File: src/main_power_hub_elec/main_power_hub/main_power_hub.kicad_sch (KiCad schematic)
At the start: 43 parts, among them J101 SM02B-PASS, J6 IDC6, U102 TCAN1462V, U2 STM32G474RBT6, U4 24LC128, Y1 24MHz

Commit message: finish fixing footprints and silkscreen
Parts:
- C11, C15, C32, C33: footprint (none) -> Capacitor_SMD:C_0402_1005Metric
- D1, D13, D14, D15, D16, D2: footprint LED_SMD:LED_WS2812B-2020_PLCC4_2.0x2.0mm -> Bluesat:WS2812B-2020
- U2: footprint Package_QFP:LQFP-64-1EP_10x10mm_P0.5mm_EP5x5mm -> Bluesat:LQFP-64-0.5
- U2: footprint Package_QFP:LQFP-64_10x10mm_P0.5mm -> Bluesat:LQFP-64-0.5
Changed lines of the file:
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@@
 			)
 		)
-		(property "Footprint" "Package_QFP:LQFP-64-1EP_10x10mm_P0.5mm_EP5x5mm"
+		(property "Footprint" "Bluesat:LQFP-64-0.5"
 			(at 132.334 24.384 0)
 			(effects
@@
 			)
 		)
-		(property "Footprint" "LED_SMD:LED_WS2812B-2020_PLCC4_2.0x2.0mm"
+		(property "Footprint" "Bluesat:WS2812B-2020"
 			(at 240.03 144.78 0)
 			(effects
@@
 			)
 		)
-		(property "Footprint" ""
+		(property "Footprint" "Capacitor_SMD:C_0402_1005Metric"
 			(at 162.56 110.49 0)
 			(effects
@@
 			)
 		)
-		(property "Footprint" ""
+		(property "Footprint" "Capacitor_SMD:C_0402_1005Metric"
 			(at 162.56 68.58 0)
 			(effects
@@
 			)
 		)
-		(property "Footprint" "LED_SMD:LED_WS2812B-2020_PLCC4_2.0x2.0mm"
+		(property "Footprint" "Bluesat:WS2812B-2020"
 			(at 207.01 144.78 0)
 			(effects
@@
 			)
 		)
-		(property "Footprint" "LED_SMD:LED_WS2812B-2020_PLCC4_2.0x2.0mm"
+		(property "Footprint" "Bluesat:WS2812B-2020"
 			(at 223.52 144.78 0)
 			(effects
@@
 			)
 		)
-		(property "Footprint" "LED_SMD:LED_WS2812B-2020_PLCC4_2.0x2.0mm"
+		(property "Footprint" "Bluesat:WS2812B-2020"
 			(at 190.5 144.78 0)
 			(effects
@@
 			)
 		)
-		(property "Footprint" "Package_QFP:LQFP-64_10x10mm_P0.5mm"
+		(property "Footprint" "Bluesat:LQFP-64-0.5"
 			(at 250.444 33.274 0)
 			(effects
@@
 			)
 		)
-		(property "Footprint" ""
+		(property "Footprint" "Capacitor_SMD:C_0402_1005Metric"
 			(at 162.56 49.53 0)
 			(effects
@@
 			)
 		)
-		(property "Footprint" "LED_SMD:LED_WS2812B-2020_PLCC4_2.0x2.0mm"
+		(property "Footprint" "Bluesat:WS2812B-2020"
 			(at 256.54 144.78 0)
 			(effects
@@
 			)
 		)
-		(property "Footprint" ""
+		(property "Footprint" "Capacitor_SMD:C_0402_1005Metric"
 			(at 162.56 88.9 0)
 			(effects
@@
 			)
 		)
-		(property "Footprint" "LED_SMD:LED_WS2812B-2020_PLCC4_2.0x2.0mm"
+		(property "Footprint" "Bluesat:WS2812B-2020"
 			(at 173.99 144.78 0)
 			(effects

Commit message: Perfect DRC pass, no errors
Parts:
- removed D10: D_TVS_Dual_Compact, Package_DFN_QFN:Diodes_UDFN-10_1.0x2.5mm_P0.5mm, symbol Bluesat:D_TVS_Quad_Compact
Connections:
- no-connect marks 1 -> 5
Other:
- note added: "TVS WAS HERE RIP"
- note removed: "change TVS during layout whats easiest"
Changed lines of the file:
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@@
 		)
 	)
-	(text "change TVS during layout\nwhats easiest"
+	(text "TVS WAS HERE\nRIP"
 		(exclude_from_sim no)
-		(at 46.99 96.266 0)
+		(at 44.704 88.9 0)
 		(effects
 			(font
@@
 	)
 	(no_connect
+		(at 45.72 83.82)
+	)
+	(no_connect
+		(at 48.26 83.82)
+	)
+	(no_connect
 		(at 262.89 137.16)
 	)
+	(no_connect
+		(at 40.64 83.82)
+	)
+	(no_connect
+		(at 43.18 83.82)
+	)
 	(bus_entry
 		(at 33.02 69.85)
@@
 	(wire
 		(pts
-			(xy 44.45 97.79) (xy 44.45 91.44)
-		)
-		(stroke
-			(width 0)
-			(type default)
-		)
-	)
-	(wire
-		(pts
 			(xy 205.74 128.27) (xy 222.25 128.27)
 		)
@@
 	)
 	(symbol
-		(lib_id "Bluesat:D_TVS_Quad_Compact")
-		(at 44.45 87.63 0)
-		(unit 1)
-		(exclude_from_sim no)
-		(in_bom yes)
-		(on_board yes)
-		(dnp no)
-		(property "Reference" "D10"
-			(at 35.306 89.662 0)
-			(effects
-				(font
-					(size 1.016 1.016)
-				)
-				(justify left)
-			)
-		)
-		(property "Value" "D_TVS_Dual_Compact"
-			(at 35.306 92.202 0)
-			(effects
-				(font
-					(size 1.016 1.016)
-				)
-				(justify left)
-			)
-		)
-		(property "Footprint" "Package_DFN_QFN:Diodes_UDFN-10_1.0x2.5mm_P0.5mm"
-			(at 44.45 87.63 0)
-			(effects
-				(font
-					(size 1.27 1.27)
-				)
-				(hide yes)
-			)
-		)
-		(property "Datasheet" "~"
-			(at 44.45 87.63 0)
-			(effects
-				(font
-					(size 1.27 1.27)
-				)
-				(hide yes)
-			)
-		)
-		(property "Description" "Dual bidirectional transient-voltage-suppression diode, compact symbol"
-			(at 44.45 87.63 0)
-			(effects
-				(font
-					(size 1.27 1.27)
-				)
-				(hide yes)
-			)
-		)
-		(pin "10"
-		)
-		(pin "3"
-		)
-		(pin "9"
-		)
-		(pin "2"
-		)
-		(pin "1"
-		)
-		(pin "6"
-		)
-		(pin "5"
-		)
-		(pin "4"
-		)
-		(pin "8"
-		)
-		(pin "7"
-		)
-		(instances
-			(project "main_power_hub"
-				(path "/535f321e-8428-4dab-8e55-8d6d7e9876bc"
-					(reference "D10")
-					(unit 1)
-				)
-			)
-		)
-	)
-	(symbol
 		(lib_id "Device:Crystal_GND24_Small")
 		(at 99.06 57.15 270)
@@
 					(unit 1)
 				)
-			)
-		)
-	)
-	(symbol
-		(lib_id "power:GND")
-		(at 44.45 97.79 0)
-		(unit 1)
-		(exclude_from_sim no)
-		(in_bom yes)
-		(on_board yes)
-		(dnp no)
-		(fields_autoplaced yes)
-		(property "Reference" "#PWR046"
-			(at 44.45 104.14 0)
-			(effects
-				(font
-					(size 1.27 1.27)
-				)
-				(hide yes)
-			)
-		)
-		(property "Value" "GND"
-			(at 44.45 102.87 0)
-			(effects
-				(font
-					(size 1.27 1.27)
-				)
-			)
-		)
-		(property "Footprint" ""
-			(at 44.45 97.79 0)
-			(effects
-				(font
-					(size 1.27 1.27)
-				)
-				(hide yes)
-			)
-		)
-		(property "Datasheet" ""
-			(at 44.45 97.79 0)
-			(effects
-				(font
-					(size 1.27 1.27)
-				)
-				(hide yes)
-			)
-		)
-		(property "Description" "Power symbol creates a global label with name \"GND\" , ground"
-			(at 44.45 97.79 0)
-			(effects
-				(font
-					(size 1.27 1.27)
-				)
-				(hide yes)
-			)
-		)
-		(pin "1"
-		)
-		(instances
-			(project "main_power_hub"
-				(path "/535f321e-8428-4dab-8e55-8d6d7e9876bc"
-					(reference "#PWR046")
-					(unit 1)
-				)

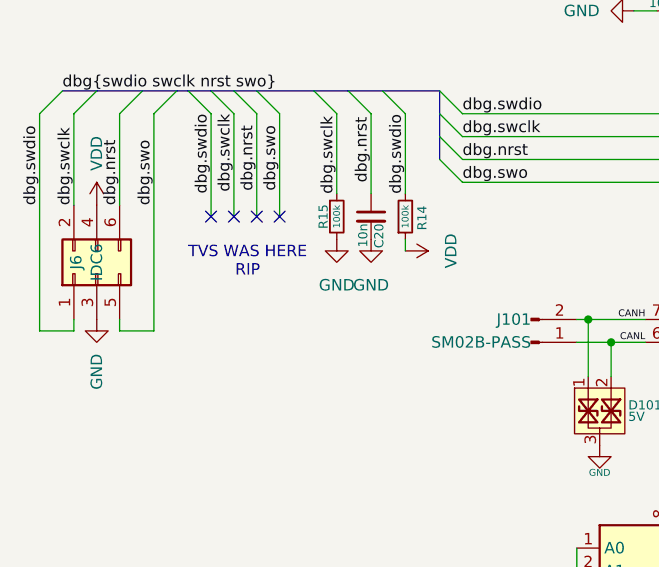
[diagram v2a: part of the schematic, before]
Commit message: TVS Diode back
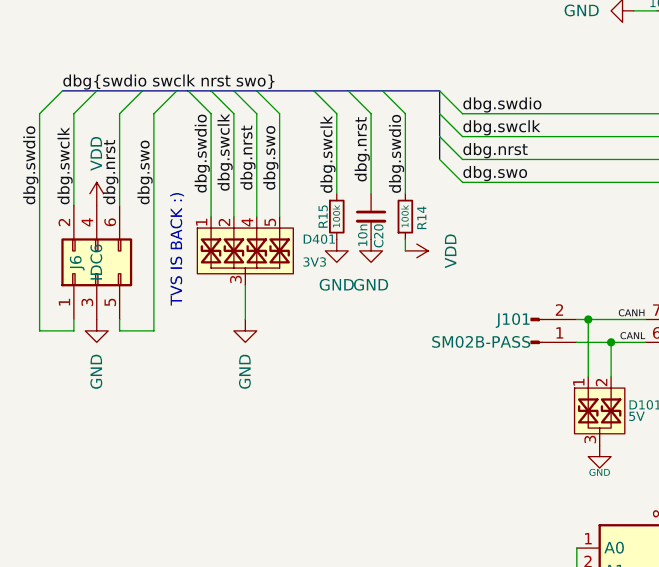
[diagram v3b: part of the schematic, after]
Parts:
- added D401: 3V3, Package_DFN_QFN:Diodes_UDFN-10_1.0x2.5mm_P0.5mm, symbol Bluesat:D_TVS_Quad_Compact
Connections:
- net GND: now also D401.3, D401.8
- net dbg.nrst: now also D401.4, D401.7
- net dbg.swclk: now also D401.2, D401.9
- net dbg.swdio: now also D401.1, D401.10
- net dbg.swo: now also D401.5, D401.6
- no-connect marks 5 -> 1
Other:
- note added: "TVS IS BACK :)"
- note removed: "TVS WAS HERE RIP"
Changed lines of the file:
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@@
 		)
 	)
-	(text "TVS WAS HERE\nRIP"
+	(text "TVS IS BACK :)"
 		(exclude_from_sim no)
-		(at 44.704 88.9 0)
+		(at 36.83 87.63 90)
 		(effects
 			(font
@@
 	)
 	(no_connect
-		(at 45.72 83.82)
-	)
-	(no_connect
-		(at 48.26 83.82)
-	)
-	(no_connect
 		(at 262.89 137.16)
 	)
-	(no_connect
-		(at 40.64 83.82)
-	)
-	(no_connect
-		(at 43.18 83.82)
-	)
 	(bus_entry
 		(at 33.02 69.85)
@@
 	(wire
 		(pts
+			(xy 44.45 95.25) (xy 44.45 91.44)
+		)
+		(stroke
+			(width 0)
+			(type default)
+		)
+	)
+	(wire
+		(pts
 			(xy 246.38 137.16) (xy 247.65 137.16)
 		)
@@
 	)
 	(symbol
+		(lib_id "Bluesat:D_TVS_Quad_Compact")
+		(at 44.45 87.63 0)
+		(unit 1)
+		(exclude_from_sim no)
+		(in_bom yes)
+		(on_board yes)
+		(dnp no)
+		(property "Reference" "D401"
+			(at 50.8 86.3599 0)
+			(effects
+				(font
+					(size 1.016 1.016)
+				)
+				(justify left)
+			)
+		)
+		(property "Value" "3V3"
+			(at 50.8 88.8999 0)
+			(effects
+				(font
+					(size 1.016 1.016)
+				)
+				(justify left)
+			)
+		)
+		(property "Footprint" "Package_DFN_QFN:Diodes_UDFN-10_1.0x2.5mm_P0.5mm"
+			(at 44.45 87.63 0)
+			(effects
+				(font
+					(size 1.27 1.27)
+				)
+				(hide yes)
+			)
+		)
+		(property "Datasheet" "~"
+			(at 44.45 87.63 0)
+			(effects
+				(font
+					(size 1.27 1.27)
+				)
+				(hide yes)
+			)
+		)
+		(property "Description" "Dual bidirectional transient-voltage-suppression diode, compact symbol"
+			(at 44.45 87.63 0)
+			(effects
+				(font
+					(size 1.27 1.27)
+				)
+				(hide yes)
+			)
+		)
+		(pin "2"
+		)
+		(pin "10"
+		)
+		(pin "3"
+		)
+		(pin "1"
+		)
+		(pin "4"
+		)
+		(pin "8"
+		)
+		(pin "7"
+		)
+		(pin "9"
+		)
+		(pin "6"
+		)
+		(pin "5"
+		)
+		(instances
+			(project "main_power_hub"
+				(path "/535f321e-8428-4dab-8e55-8d6d7e9876bc"
+					(reference "D401")
+					(unit 1)
+				)
+			)
+		)
+	)
+	(symbol
 		(lib_id "Device:Crystal_GND24_Small")
 		(at 99.06 57.15 270)
@@
 					(unit 1)
 				)
+			)
+		)
+	)
+	(symbol
+		(lib_id "power:GND")
+		(at 44.45 95.25 0)
+		(unit 1)
+		(exclude_from_sim no)
+		(in_bom yes)
+		(on_board yes)
+		(dnp no)
+		(fields_autoplaced yes)
+		(property "Reference" "#PWR0101"
+			(at 44.45 101.6 0)
+			(effects
+				(font
+					(size 1.27 1.27)
+				)
+				(hide yes)
+			)
+		)
+		(property "Value" "GND"
+			(at 44.4499 99.06 90)
+			(effects
+				(font
+					(size 1.27 1.27)
+				)
+				(justify right)
+			)
+		)
+		(property "Footprint" ""
+			(at 44.45 95.25 0)
+			(effects
+				(font
+					(size 1.27 1.27)
+				)
+				(hide yes)
+			)
+		)
+		(property "Datasheet" ""
+			(at 44.45 95.25 0)
+			(effects
+				(font
+					(size 1.27 1.27)
+				)
+				(hide yes)
+			)
+		)
+		(property "Description" "Power symbol creates a global label with name \"GND\" , ground"
+			(at 44.45 95.25 0)
+			(effects
+				(font
+					(size 1.27 1.27)
+				)
+				(hide yes)
+			)
+		)
+		(pin "1"
+		)
+		(instances
+			(project "main_power_hub"
+				(path "/535f321e-8428-4dab-8e55-8d6d7e9876bc"
+					(reference "#PWR0101")
+					(unit 1)
+				)

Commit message: Update swdebug header
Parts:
- added H1, H2: MountingHole, Bluesat:M2.5, symbol Mechanical:MountingHole
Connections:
- net dbg.nrst: now also J6.5 (Pin_5); no longer J6.6 (Pin_6)
- net dbg.swclk: now also J6.1 (Pin_1); no longer J6.2 (Pin_2)
- net dbg.swdio: now also J6.2 (Pin_2); no longer J6.1 (Pin_1)
- net dbg.swo: now also J6.6 (Pin_6); no longer J6.5 (Pin_5)
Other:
- moved on the sheet: J6

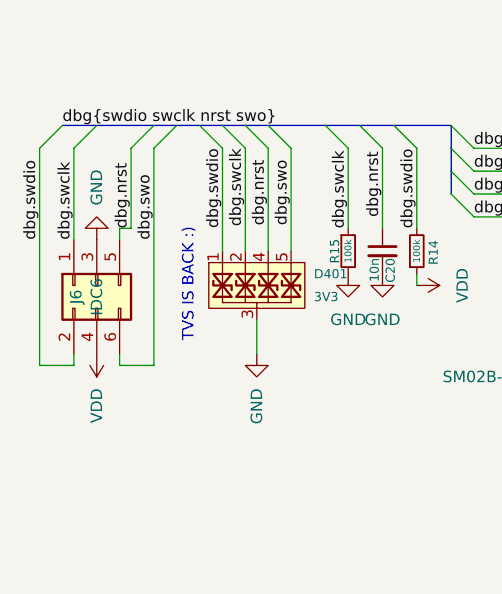
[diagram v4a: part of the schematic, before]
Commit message: Fix IDC6 pinout
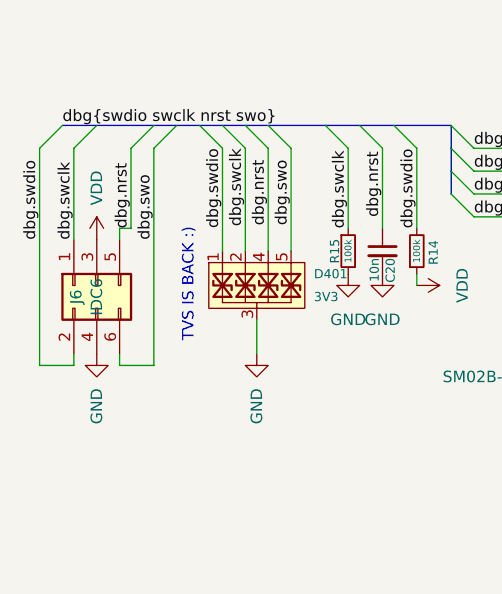
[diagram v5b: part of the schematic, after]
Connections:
- net GND: now also J6.4 (Pin_4); no longer J6.3 (Pin_3)
- net VDD: now also J6.3 (Pin_3); no longer J6.4 (Pin_4)
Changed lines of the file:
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@@
 	(symbol
 		(lib_id "power:GND")
-		(at 26.67 82.55 0)
-		(mirror x)
+		(at 26.67 95.25 0)
 		(unit 1)
 		(exclude_from_sim no)
@@
 		(fields_autoplaced yes)
 		(property "Reference" "#PWR036"
-			(at 26.67 76.2 0)
+			(at 26.67 101.6 0)
 			(effects
 				(font
@@
 		)
 		(property "Value" "GND"
-			(at 26.6699 78.74 90)
+			(at 26.6699 99.06 90)
 			(effects
 				(font
@@
 		)
 		(property "Footprint" ""
-			(at 26.67 82.55 0)
+			(at 26.67 95.25 0)
 			(effects
 				(font
@@
 		)
 		(property "Datasheet" ""
-			(at 26.67 82.55 0)
+			(at 26.67 95.25 0)
 			(effects
 				(font
@@
 		)
 		(property "Description" "Power symbol creates a global label with name \"GND\" , ground"
-			(at 26.67 82.55 0)
+			(at 26.67 95.25 0)
 			(effects
 				(font
@@
 	(symbol
 		(lib_id "power:VDD")
-		(at 26.67 95.25 0)
-		(mirror x)
+		(at 26.67 82.55 0)
 		(unit 1)
 		(exclude_from_sim no)
@@
 		(fields_autoplaced yes)
 		(property "Reference" "#PWR037"
-			(at 26.67 91.44 0)
+			(at 26.67 86.36 0)
 			(effects
 				(font
@@
 		)
 		(property "Value" "VDD"
-			(at 26.6699 99.06 90)
+			(at 26.6699 78.74 90)
 			(effects
 				(font
@@
 		)
 		(property "Footprint" ""
-			(at 26.67 95.25 0)
+			(at 26.67 82.55 0)
 			(effects
 				(font
@@
 		)
 		(property "Datasheet" ""
-			(at 26.67 95.25 0)
+			(at 26.67 82.55 0)
 			(effects
 				(font
@@
 		)
 		(property "Description" "Power symbol creates a global label with name \"VDD\""
-			(at 26.67 95.25 0)
+			(at 26.67 82.55 0)
 			(effects
 				(font

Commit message: Use bluesat TSSOP8 footprint
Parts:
- U4: footprint Package_SO:TSSOP-8_4.4x3mm_P0.65mm -> Bluesat:TSSOP-8_4.4x3.0-0.65
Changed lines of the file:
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@@
 			)
 		)
-		(property "Footprint" "Package_SO:TSSOP-8_4.4x3mm_P0.65mm"
+		(property "Footprint" "Bluesat:TSSOP-8_4.4x3.0-0.65"
 			(at 91.44 123.19 0)
 			(effects

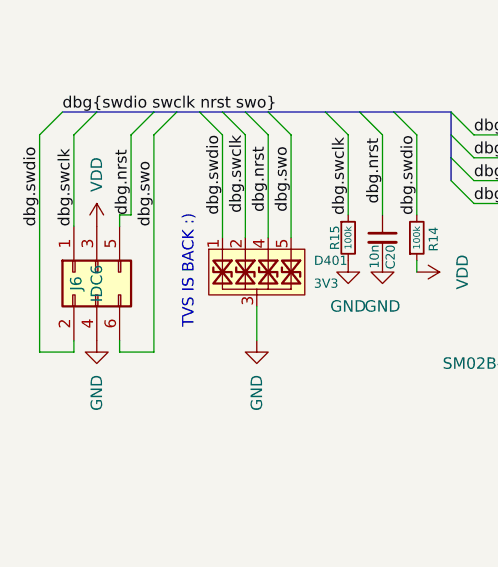
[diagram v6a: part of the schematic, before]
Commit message: Fix rotated IDC6 on CPM/MPM/VESC/Stepper/USB Hub (#120)
* Fix rotated IDC6 on CPM/MPM/VESC/Stepper/USB Hub

* Fix VESC
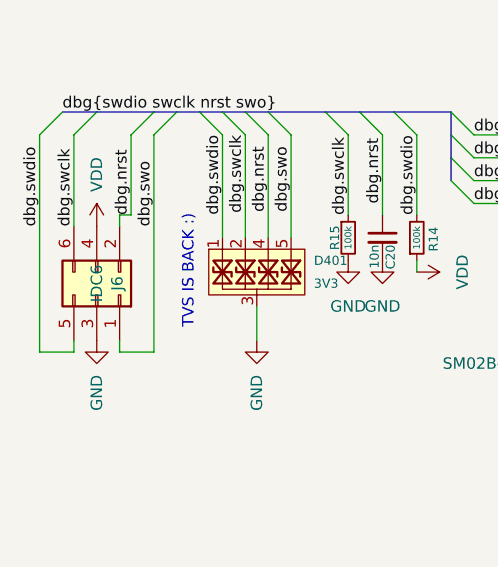
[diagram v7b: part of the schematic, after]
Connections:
- net GND: now also J6.3 (Pin_3); no longer J6.4 (Pin_4)
- net VDD: now also J6.4 (Pin_4); no longer J6.3 (Pin_3)
- net dbg.nrst: now also J6.2 (Pin_2); no longer J6.5 (Pin_5)
- net dbg.swclk: now also J6.6 (Pin_6); no longer J6.1 (Pin_1)
- net dbg.swdio: now also J6.5 (Pin_5); no longer J6.2 (Pin_2)
- net dbg.swo: now also J6.1 (Pin_1); no longer J6.6 (Pin_6)
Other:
- moved on the sheet: J6
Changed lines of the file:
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@@
+	(wire
+		(pts
+			(xy 62.23 72.39) (xy 62.23 81.28)
+		)
+		(stroke
+			(width 0)
+			(type default)
+		)
+	)
+	(wire
+		(pts
+			(xy 67.31 158.75) (xy 67.31 161.29)
+		)
+		(stroke
+			(width 0)
+			(type default)
+		)
+	)
+	(wire
+		(pts
+			(xy 157.48 41.91) (xy 193.04 41.91)
+		)
+		(stroke
+			(width 0)
+			(type default)
+		)
+	)
+	(wire
+		(pts
+			(xy 85.09 158.75) (xy 85.09 161.29)
+		)
+		(stroke
+			(width 0)
+			(type default)
+		)
+	)
+	(wire
+		(pts
+			(xy 99.06 60.96) (xy 100.33 60.96)
+		)
+		(stroke
+			(width 0)
+			(type default)
+		)
+	)
+	(wire
+		(pts
+			(xy 240.03 53.34) (xy 240.03 55.88)
+		)
+		(stroke
+			(width 0)
+			(type default)
+		)
+	)
+	(wire
+		(pts
+			(xy 62.23 87.63) (xy 62.23 86.36)
+		)
+		(stroke
+			(width 0)
+			(type default)
+		)
+	)
+	(wire
+		(pts
+			(xy 240.03 55.88) (xy 240.03 58.42)
+		)
+		(stroke
+			(width 0)
+			(type default)
+		)
+	)
+	(bus
+		(pts
+			(xy 66.04 69.85) (xy 66.04 72.39)
+		)
+		(stroke
+			(width 0)
+			(type default)
+		)
+	)
+	(wire
+		(pts
+			(xy 71.12 158.75) (xy 71.12 161.29)
+		)
+		(stroke
+			(width 0)
+			(type default)
+		)
+	)
+	(wire
+		(pts
+			(xy 59.69 158.75) (xy 59.69 161.29)
+		)
+		(stroke
+			(width 0)
+			(type default)
+		)
+	)
+	(wire
+		(pts
+			(xy 264.16 128.27) (xy 255.27 128.27)
+		)
+		(stroke
+			(width 0)
+			(type default)
+		)
+	)
+	(wire
+		(pts
+			(xy 55.88 158.75) (xy 55.88 161.29)
+		)
+		(stroke
+			(width 0)
+			(type default)
+		)
+	)
+	(wire
+		(pts
+			(xy 265.43 50.8) (xy 265.43 53.34)
+		)
+		(stroke
+			(width 0)
+			(type default)
+		)
+	)
+	(wire
+		(pts
+			(xy 87.63 60.96) (xy 90.17 60.96)
+		)
+		(stroke
+			(width 0)
+			(type default)
+		)
+	)
+	(wire
+		(pts
+			(xy 238.76 144.78) (xy 238.76 146.05)
+		)
+		(stroke
+			(width 0)
+			(type default)
+		)
+	)
+	(wire
+		(pts
+			(xy 85.09 158.75) (xy 88.9 158.75)
+		)
+		(stroke
+			(width 0)
+			(type default)
+		)
+	)
+	(wire
+		(pts
+			(xy 157.48 113.03) (xy 165.1 113.03)
+		)
+		(stroke
+			(width 0)
+			(type default)
+		)
+	)
+	(wire
+		(pts
+			(xy 101.6 123.19) (xy 105.41 123.19)
+		)
+		(stroke
+			(width 0)
+			(type default)
+		)
+	)
+	(wire
+		(pts
+			(xy 81.28 120.65) (xy 81.28 123.19)
+		)
+		(stroke
+			(width 0)
+			(type default)
+		)
+	)
+	(bus
+		(pts
+			(xy 66.04 72.39) (xy 66.04 74.93)
+		)
+		(stroke
+			(width 0)
+			(type default)
+		)
+	)
+	(wire
+		(pts
+			(xy 81.28 123.19) (xy 81.28 125.73)
+		)
+		(stroke
+			(width 0)
+			(type default)
+		)
+	)
+	(wire
+		(pts
+			(xy 157.48 86.36) (xy 193.04 86.36)
+		)
+		(stroke
+			(width 0)
+			(type default)
+		)
+	)
+	(wire
+		(pts
+			(xy 40.64 72.39) (xy 40.64 83.82)
+		)
+		(stroke
+			(width 0)
+			(type default)
+		)
+	)
 	(wire
 		(pts
 			(xy 24.13 72.39) (xy 24.13 82.55)
-		)
-		(stroke
-			(width 0)
-			(type default)
-		)
-	)
-	(wire
-		(pts
-			(xy 62.23 72.39) (xy 62.23 81.28)
-		)
-		(stroke
-			(width 0)
-			(type default)
-		)
-	)
-	(wire
-		(pts
-			(xy 67.31 158.75) (xy 67.31 161.29)
-		)
-		(stroke
-			(width 0)
-			(type default)
-		)
-	)
-	(wire
-		(pts
-			(xy 157.48 41.91) (xy 193.04 41.91)
-		)
-		(stroke
-			(width 0)
-			(type default)
-		)
-	)
-	(wire
-		(pts
-			(xy 85.09 158.75) (xy 85.09 161.29)
-		)
-		(stroke
-			(width 0)
-			(type default)
-		)
-	)
-	(wire
-		(pts
-			(xy 99.06 60.96) (xy 100.33 60.96)
-		)
-		(stroke
-			(width 0)
-			(type default)
-		)
-	)
-	(wire
-		(pts
-			(xy 240.03 53.34) (xy 240.03 55.88)
-		)
-		(stroke
-			(width 0)
-			(type default)
-		)
-	)
-	(wire
-		(pts
-			(xy 62.23 87.63) (xy 62.23 86.36)
-		)
-		(stroke
-			(width 0)
-			(type default)
-		)
-	)
-	(wire
-		(pts
-			(xy 240.03 55.88) (xy 240.03 58.42)
-		)
-		(stroke
-			(width 0)
-			(type default)
-		)
-	)
-	(bus
-		(pts
-			(xy 66.04 69.85) (xy 66.04 72.39)
-		)
-		(stroke
-			(width 0)
-			(type default)
-		)
-	)
-	(wire
-		(pts
-			(xy 71.12 158.75) (xy 71.12 161.29)
-		)
-		(stroke
-			(width 0)
-			(type default)
-		)
-	)
-	(wire
-		(pts
-			(xy 59.69 158.75) (xy 59.69 161.29)
-		)
-		(stroke
-			(width 0)
-			(type default)
-		)
-	)
-	(wire
-		(pts
-			(xy 264.16 128.27) (xy 255.27 128.27)
-		)
-		(stroke
-			(width 0)
-			(type default)
-		)
-	)
-	(wire
-		(pts
-			(xy 55.88 158.75) (xy 55.88 161.29)
-		)
-		(stroke
-			(width 0)
-			(type default)
-		)
-	)
-	(wire
-		(pts
-			(xy 265.43 50.8) (xy 265.43 53.34)
-		)
-		(stroke
-			(width 0)
-			(type default)
-		)
-	)
-	(wire
-		(pts
-			(xy 87.63 60.96) (xy 90.17 60.96)
-		)
-		(stroke
-			(width 0)
-			(type default)
-		)
-	)
-	(wire
-		(pts
-			(xy 238.76 144.78) (xy 238.76 146.05)
-		)
-		(stroke
-			(width 0)
-			(type default)
-		)
-	)
-	(wire
-		(pts
-			(xy 85.09 158.75) (xy 88.9 158.75)
-		)
-		(stroke
-			(width 0)
-			(type default)
-		)
-	)
-	(wire
-		(pts
-			(xy 157.48 113.03) (xy 165.1 113.03)
-		)
-		(stroke
-			(width 0)
-			(type default)
-		)
-	)
-	(wire
-		(pts
-			(xy 101.6 123.19) (xy 105.41 123.19)
-		)
-		(stroke
-			(width 0)
-			(type default)
-		)
-	)
-	(wire
-		(pts
-			(xy 81.28 120.65) (xy 81.28 123.19)
-		)
-		(stroke
-			(width 0)
-			(type default)
-		)
-	)
-	(bus
-		(pts
-			(xy 66.04 72.39) (xy 66.04 74.93)
-		)
-		(stroke
-			(width 0)
-			(type default)
-		)
-	)
-	(wire
-		(pts
-			(xy 81.28 123.19) (xy 81.28 125.73)
-		)
-		(stroke
-			(width 0)
-			(type default)
-		)
-	)
-	(wire
-		(pts
-			(xy 157.48 86.36) (xy 193.04 86.36)
-		)
-		(stroke
-			(width 0)
-			(type default)
-		)
-	)
-	(wire
-		(pts
-			(xy 40.64 72.39) (xy 40.64 83.82)
 		)
 		(stroke
@@
 	(symbol
 		(lib_id "Connector_Generic:Conn_02x03_Odd_Even")
-		(at 26.67 87.63 90)
+		(at 26.67 90.17 270)
 		(mirror x)
 		(unit 1)
@@
 		(dnp no)
 		(property "Reference" "J6"
-			(at 24.384 88.9 0)
+			(at 28.956 88.9 0)
 			(effects
 				(font
@@
 		)
 		(property "Footprint" "Bluesat:IDC6"
-			(at 26.67 87.63 0)
+			(at 26.67 90.17 0)
 			(effects
 				(font
@@
 		)
 		(property "Datasheet" "~"
-			(at 26.67 87.63 0)
+			(at 26.67 90.17 0)
 			(effects
 				(font
@@
 		)
 		(property "Description" "Generic connector, double row, 02x03, odd/even pin numbering scheme (row 1 odd numbers, row 2 even numbers), script generated (kicad-library-utils/schlib/autogen/connector/)"
-			(at 26.67 87.63 0)
-			(effects
-				(font
+			(at 26.67 90.17 0)
+			(effects
+				(font
